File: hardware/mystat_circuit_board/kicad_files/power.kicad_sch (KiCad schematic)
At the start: 17 parts, among them J1 PJ-063AH, U2 LTM8045, U3 ADP7182AUJZ-R7, U4 ADP7118AUJZ-5.0-R7

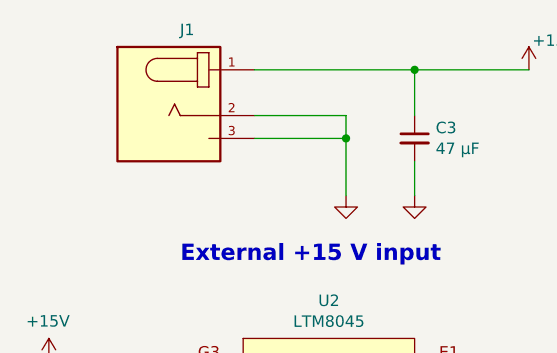
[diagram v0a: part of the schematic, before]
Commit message: Add files via upload
Minor re-routing tracks on PCB to pass KiCad 7.0 design rules checks
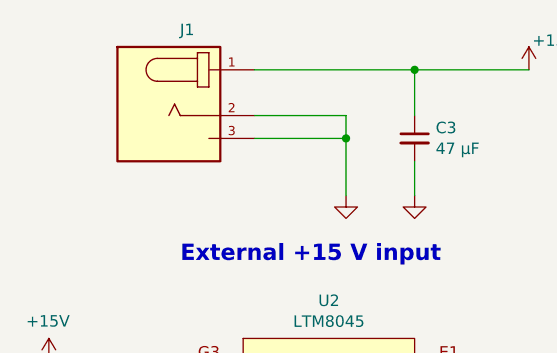
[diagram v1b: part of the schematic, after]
